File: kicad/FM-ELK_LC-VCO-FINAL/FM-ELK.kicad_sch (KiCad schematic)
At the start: 11 parts, among them Q1 BS170, Q2 BS170, Q3 BS170, Q4 BS170

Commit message: Projekt aktualisiert
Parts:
- removed L3: 3.3u, symbol Device:L
- added L1: 3.3u, symbol Device:L
- R4: value 510k -> 1500k
- Vtune1: value 6.89 -> 5.33
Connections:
- net Out: now also L2.2
- net at R4.2, Vdd1.1: now also L2.1, L1.1; no longer L2.2
- net at D1.1 (K), Q1.2 (G), Q2.1 (D): now also L1.2; no longer L2.1
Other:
- moved on the sheet: Q4, R4, Vdd1

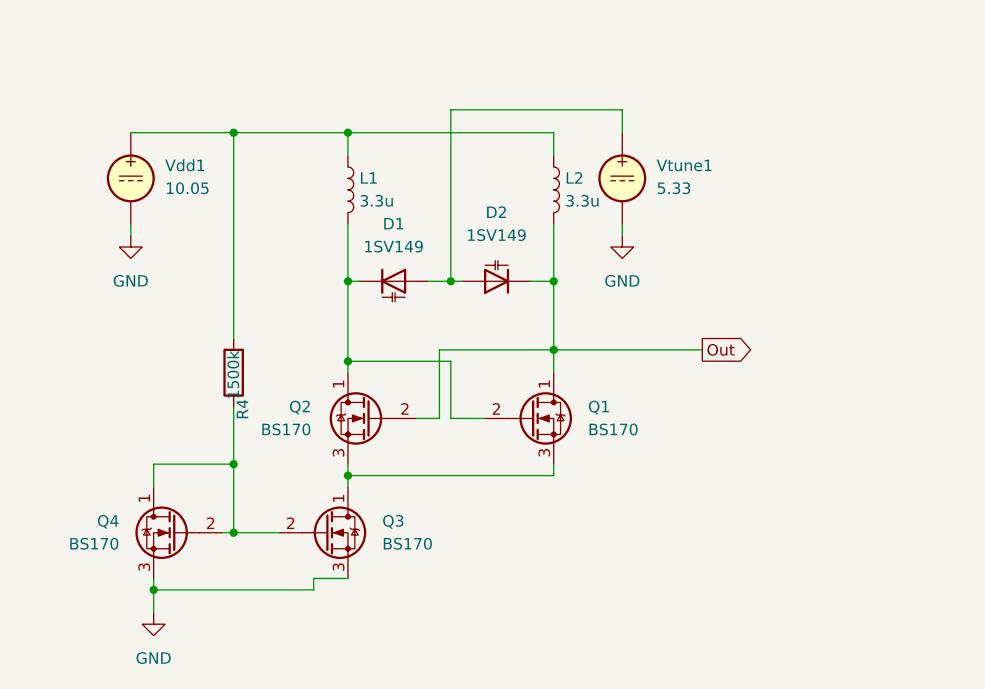
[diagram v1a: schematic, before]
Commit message: Board aktualisiert und Python angepasst
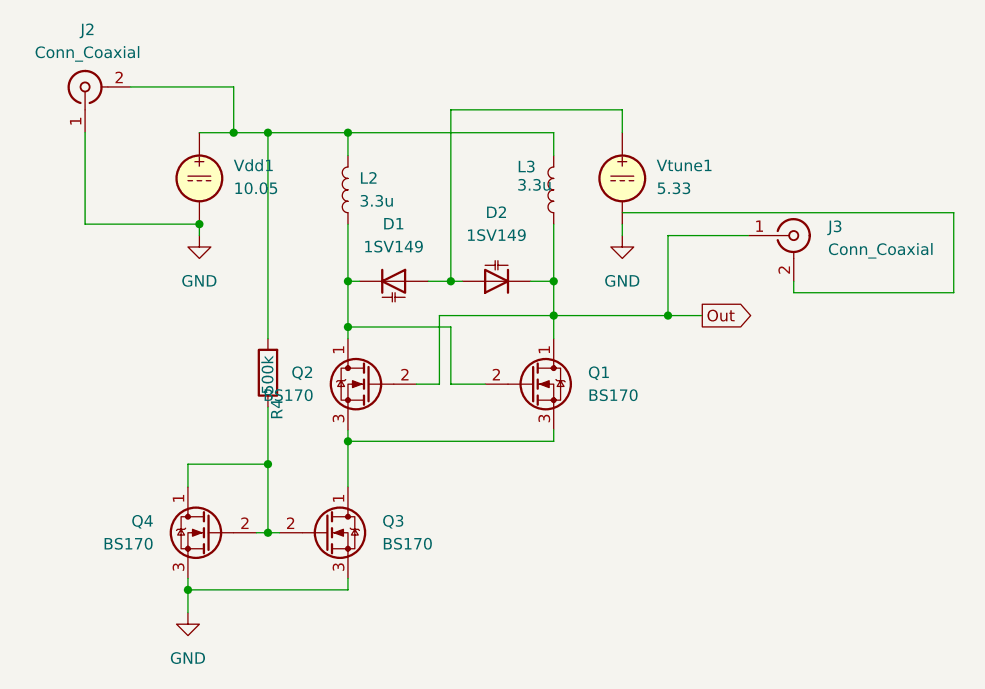
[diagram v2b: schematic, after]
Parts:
- removed L1: 3.3u, symbol Device:L
- added J2, J3: Conn_Coaxial, Connector_Coaxial:BNC_Amphenol_031-5539_Vertical, symbol Connector:Conn_Coaxial
- added L3: 3.3u, Inductor_THT:L_Radial_D10.0mm_P5.00mm_Fastron_07P, symbol Device:L
- D1, D2: footprint (none) -> Package_TO_SOT_THT:TO-92_Inline
- L2: footprint (none) -> Inductor_THT:L_Radial_D10.0mm_P5.00mm_Fastron_07P
- R4: value 1500k -> 500k; footprint (none) -> Resistor_THT:R_Axial_DIN0207_L6.3mm_D2.5mm_P7.62mm_Horizontal
- Vdd1, Vtune1: footprint (none) -> Connector_PinHeader_2.54mm:PinHeader_1x02_P2.54mm_Vertical
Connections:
- net GND: now also J2.1 (In)
- net Out: now also J3.1 (In), L3.1; no longer L2.2
- net at R4.2, Vdd1.1: now also L2.2, J2.2 (Ext), L3.2; no longer L2.1
- net at D1.1 (K), Q1.2 (G), Q2.1 (D): now also L2.1
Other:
- moved on the sheet: Q1, Q2, Q4, R4, Vdd1
